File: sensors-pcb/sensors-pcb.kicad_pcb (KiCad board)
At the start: 2 copper layers, 75 x 55 mm, 67 parts, among them J1 Network Connector, J2 STDC14, J3 Conn_Coaxial, SW1 SW_Push, U1 MAX-M8Q, U2 BNO055, U3 LD39050PU33R, U4 STM32G474RBT6, U5 SN65HVD230, Y1 32kHz, Y2 8MHz

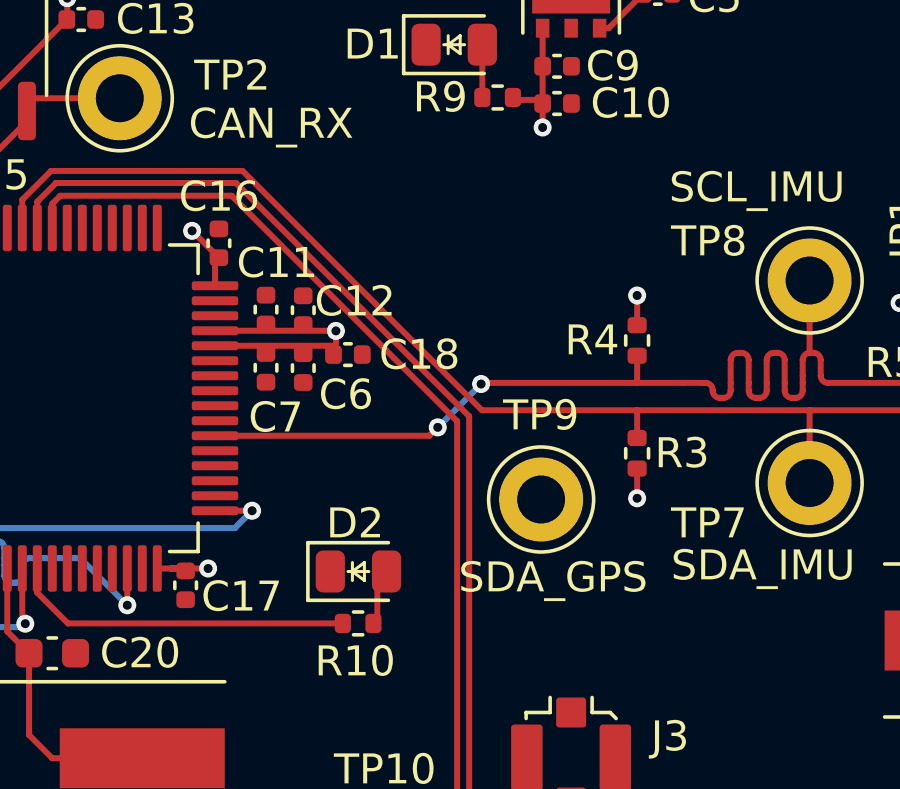
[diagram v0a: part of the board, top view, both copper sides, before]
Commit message: sensors-pcb: connector SDA_GPS test point
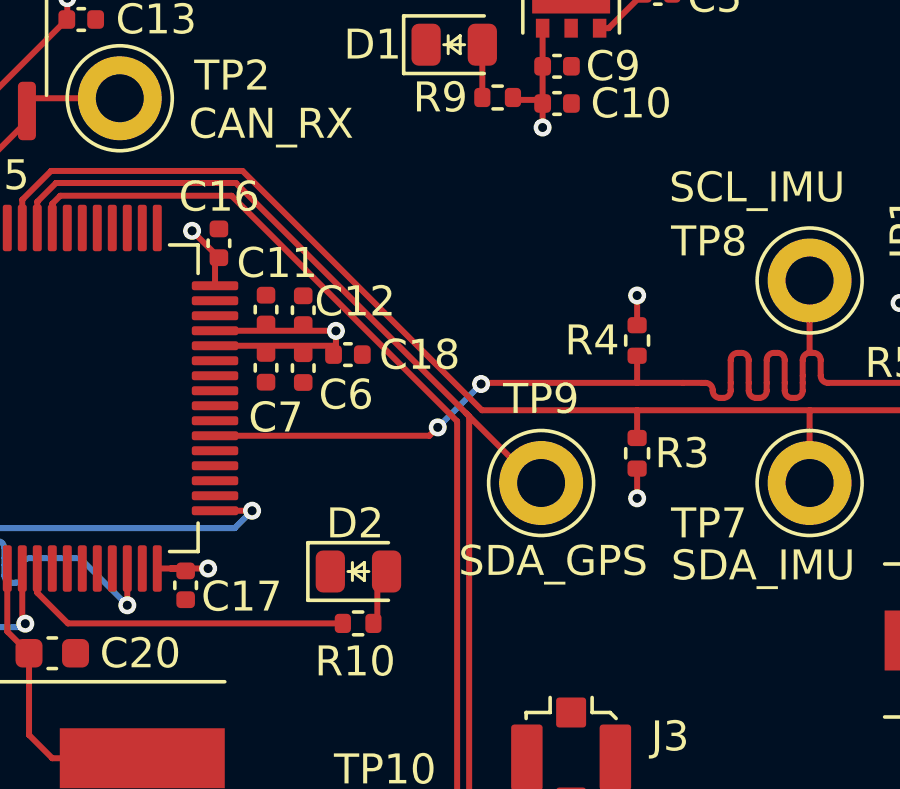
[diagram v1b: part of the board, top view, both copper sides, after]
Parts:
- moved TP9 0.55 mm to (234.8, 50.2)
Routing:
- net /SDA_GPS: track 44.6 -> 48.0 mm
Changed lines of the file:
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@@
 	(footprint "TestPoint:TestPoint_Keystone_5005-5009_Compact"
 		(layer "F.Cu")
-		(at 234.8 50.8)
+		(at 234.8 50.25)
 		(descr "Keystone THM Compact Test Point 5005-5009, http://www.keyelco.com/product-pdf.cfm?p=1314")
 		(tags "Through Hole Mount Test Points")
@@
 	)
 	(segment
+		(start 232.312325 47.937675)
+		(end 232.401 48.02635)
+		(width 0.2)
+		(layer "F.Cu")
+		(net 37)
+	)
+	(segment
 		(start 232.401 48.02635)
 		(end 232.401 64.826339)
@@
 	(segment
 		(start 224.62465 40.25)
-		(end 232.401 48.02635)
+		(end 232.312325 47.937675)
+		(width 0.2)
+		(layer "F.Cu")
+		(net 37)
+	)
+	(segment
+		(start 232.312325 47.937675)
+		(end 234.62465 50.25)
 		(width 0.2)
 		(layer "F.Cu")
@@
 		(width 0.2)
 		(layer "F.Cu")
+		(net 37)
+	)
+	(segment
+		(start 234.62465 50.25)
+		(end 234.8 50.25)
+		(width 0.2)
+		(layer "F.Cu")

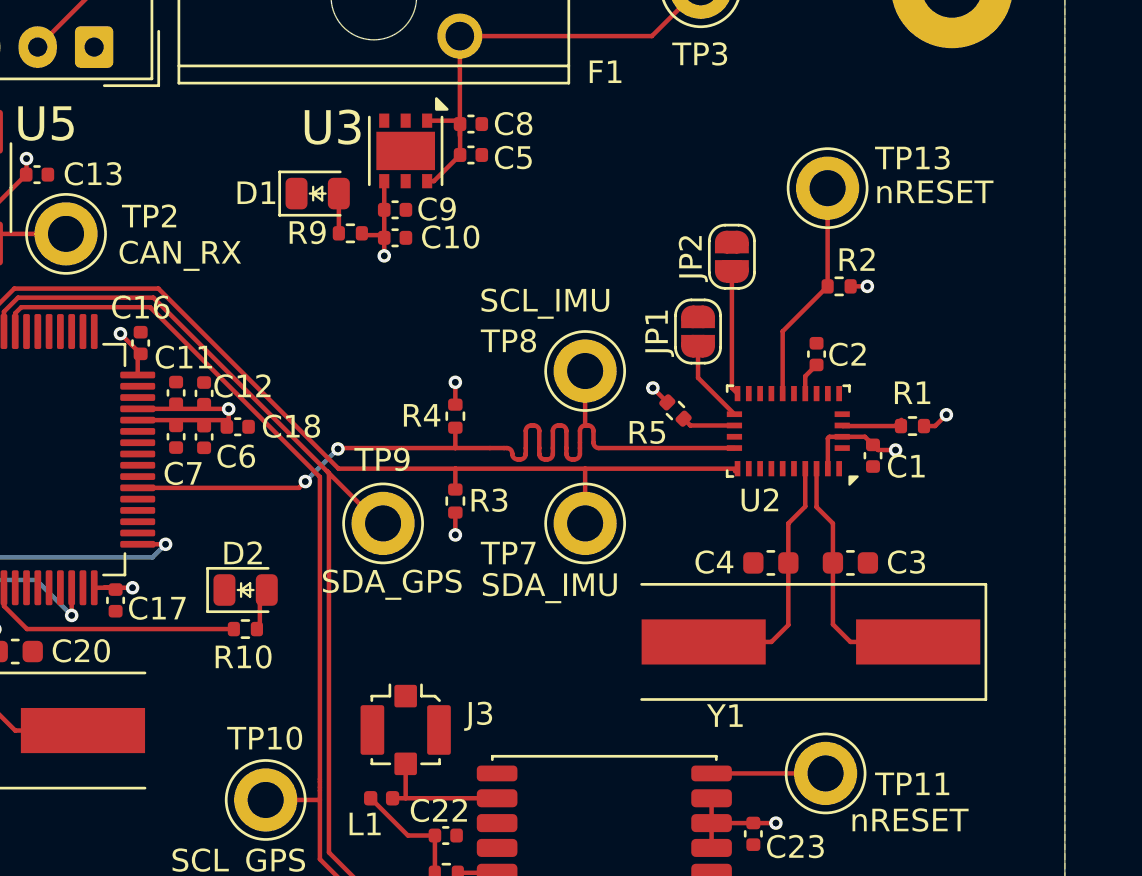
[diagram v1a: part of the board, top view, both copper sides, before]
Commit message: sensors-pcb: replace IMU with MPU-6050
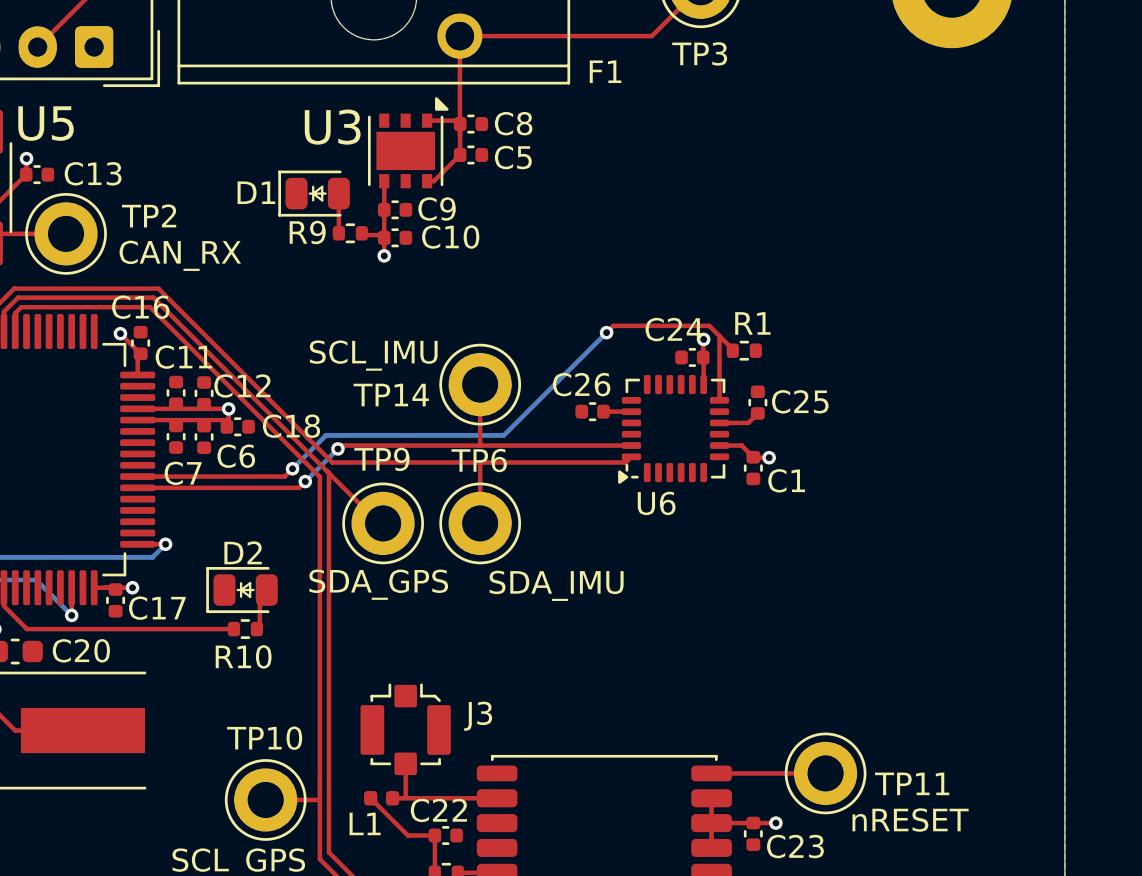
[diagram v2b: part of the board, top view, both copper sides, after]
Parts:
- removed C2: 100n, Capacitor_SMD:C_0402_1005Metric
- removed C3, C4: 22p, Capacitor_SMD:C_0603_1608Metric
- removed JP1, JP2: SolderJumper_2_Open, Jumper:SolderJumper-2_P1.3mm_Open_RoundedPad1.0x1.5mm
- removed R2, R3, R4: 10k, Resistor_SMD:R_0402_1005Metric
- removed R5: 39k, Resistor_SMD:R_0402_1005Metric
- removed TP13, TP7, TP8: TestPoint, TestPoint:TestPoint_Keystone_5005-5009_Compact
- removed U2: BNO055, Package_LGA:LGA-28_5.2x3.8mm_P0.5mm
- removed Y1: 32kHz, Exocet:Crystal_SMD_HC49-SD
- added C24: 100n, Capacitor_SMD:C_0402_1005Metric, F.Cu at (248.5, 42.9)
- added C25: 100n, Capacitor_SMD:C_0402_1005Metric, F.Cu at (251.4, 44.9)
- added C26: 2.2n, Capacitor_SMD:C_0402_1005Metric, F.Cu at (244.1, 45.3)
- added TP14: TestPoint, TestPoint:TestPoint_Keystone_5005-5009_Compact, F.Cu at (239.1, 44.1)
- added TP6: TestPoint, TestPoint:TestPoint_Keystone_5005-5009_Compact, F.Cu at (239.1, 50.2)
- added U6: MPU-6050, Sensor_Motion:InvenSense_QFN-24_4x4mm_P0.5mm, F.Cu at (247.8, 46.0)
- C1: value 100n -> 10n
- R1: value 10k -> 100k
- moved R1 8.16 mm to (250.8, 42.6)
- moved C1 5.33 mm to (251.2, 47.8), turned to 90 degrees
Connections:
- C1 pad 1: +3.3V -> GND
- C1 pad 2: GND -> +3.3V
- R1 pad 1: Net-(U2-nBOOT_LOAD_PIN) -> /INT_IMU
- R1 pad 2: +3.3V -> GND
- U4 pad 23: unconnected-(U4-PC5-Pad23) -> /INT_IMU
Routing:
- net /INT_IMU: track 0.00 -> 32.5 mm, vias 0 -> 2
- net /SCL_IMU: track 37.9 -> 25.3 mm
- net /OSC_IN: track 11.6 -> 0.00 mm
- net /OSC_OUT: track 11.6 -> 0.00 mm
- net Net-(U2-~{nReset}): track 9.92 -> 0.00 mm
- net /SDA_IMU: track 41.1 -> 35.6 mm
- net Net-(JP2-A): track 5.52 -> 0.00 mm
- net +3.3V: track 44.9 -> 39.9 mm, vias 16 -> 12
- net Net-(JP1-A): track 3.68 -> 0.00 mm
- net Net-(U2-nBOOT_LOAD_PIN): track 2.97 -> 0.00 mm
- net Net-(U2-COM3): track 2.38 -> 0.00 mm
- net Net-(U6-REGOUT): track 0.00 -> 1.87 mm
- net Net-(U2-CAP): track 1.48 -> 0.00 mm
- net Net-(U6-CPOUT): track 0.00 -> 1.24 mm

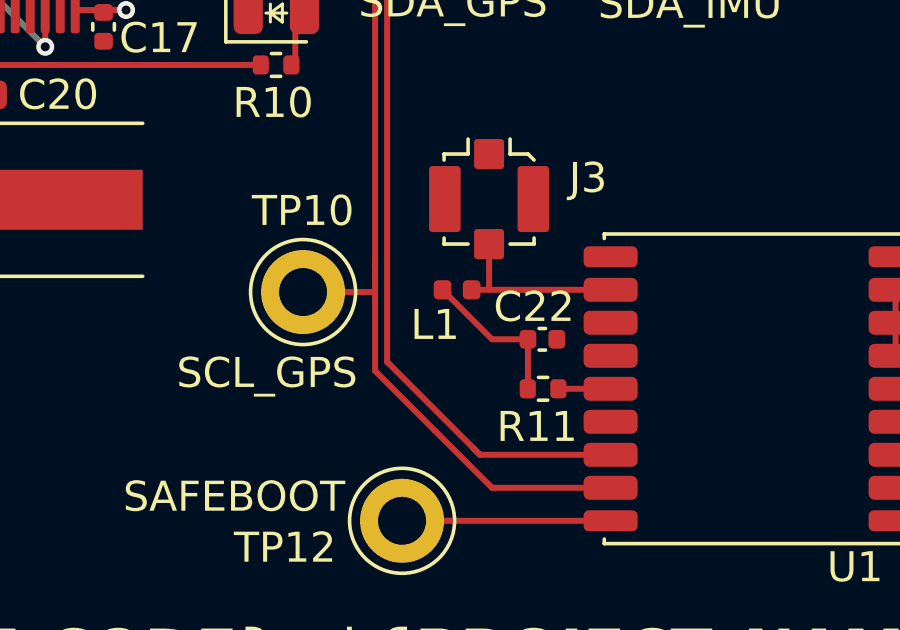
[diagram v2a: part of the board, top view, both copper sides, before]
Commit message: sensors-pcb: change 27nH to 10nH+15nH
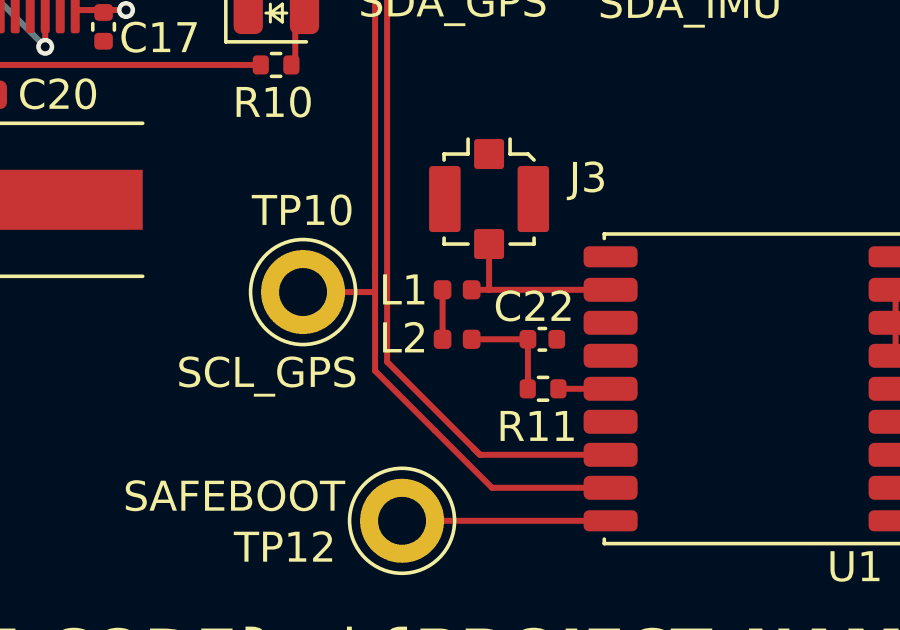
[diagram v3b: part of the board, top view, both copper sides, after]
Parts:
- added L2: 15n, Inductor_SMD:L_0402_1005Metric, F.Cu at (234.7, 64.1)
- L1: value 27n -> 10n
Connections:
- L1 pad 1: Net-(C22-Pad1) -> Net-(L1-Pad1)
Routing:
- net Net-(C22-Pad1): track 5.18 -> 3.53 mm
- net Net-(L1-Pad1): track 0.00 -> 1.65 mm
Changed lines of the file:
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@@
 	(net 94 "Net-(C22-Pad1)")
 	(net 95 "Net-(U1-~{SAFEBOOT})")
+	(net 96 "Net-(L1-Pad1)")
 	(footprint "Capacitor_SMD:C_0402_1005Metric"
 		(layer "F.Cu")
@@
 		(tags "inductor")
 		(property "Reference" "L1"
-			(at -0.735 1.175 0)
+			(at -1.785 0.025 0)
 			(layer "F.SilkS")
 			(effects
@@
 			)
 		)
-		(property "Value" "27n"
+		(property "Value" "10n"
 			(at 0 0 0)
 			(layer "F.Fab")
@@
 			)
 		)
-		(property "JLCPCB" "C12669"
+		(property "JLCPCB" "C27147"
 			(at 0 0 0)
 			(unlocked yes)
@@
 			(layers "F.Cu" "F.Mask" "F.Paste")
 			(roundrect_rratio 0.25)
-			(net 94 "Net-(C22-Pad1)")
+			(net 96 "Net-(L1-Pad1)")
 			(pinfunction "1")
 			(pintype "passive")
@@
 		)
 	)
+	(footprint "Inductor_SMD:L_0402_1005Metric"
+		(layer "F.Cu")
+		(at 234.735 64.075 180)
+		(descr "Inductor SMD 0402 (1005 Metric), square (rectangular) end terminal, IPC-7351 nominal, (Body size source: http://www.tortai-tech.com/upload/download/2011102023233369053.pdf), generated with kicad-footprint-generator")
+		(tags "inductor")
+		(property "Reference" "L2"
+			(at 1.785 0.025 0)
+			(layer "F.SilkS")
+			(effects
+				(font
+					(size 1 1)
+					(thickness 0.15)
+				)
+			)
+		)
+		(property "Value" "15n"
+			(at 0 0 0)
+			(layer "F.Fab")
+			(effects
+				(font
+					(size 1 1)
+					(thickness 0.15)
+				)
+			)
+		)
+		(property "Datasheet" "~"
+			(at 0 0 0)
+			(layer "F.Fab")
+			(hide yes)
+			(effects
+				(font
+					(size 1.27 1.27)
+					(thickness 0.15)
+				)
+			)
+		)
+		(property "Description" "Inductor"
+			(at 0 0 0)
+			(layer "F.Fab")
+			(hide yes)
+			(effects
+				(font
+					(size 1.27 1.27)
+					(thickness 0.15)
+				)
+			)
+		)
+		(property "JLCPCB" "C27143"
+			(at 0 0 180)
+			(unlocked yes)
+			(layer "F.Fab")
+			(hide yes)
+			(effects
+				(font
+					(size 1 1)
+					(thickness 0.15)
+				)
+			)
+		)
+		(property ki_fp_filters "Choke_* *Coil* Inductor_* L_*")
+		(sheetname "/")
+		(sheetfile "sensors-pcb.kicad_sch")
+		(attr smd)
+		(fp_line
+			(start 0.93 0.47)
+			(end -0.93 0.47)
+			(stroke
+				(width 0.05)
+				(type solid)
+			)
+			(layer "F.CrtYd")
+		)
+		(fp_line
+			(start 0.93 -0.47)
+			(end 0.93 0.47)
+			(stroke
+				(width 0.05)
+				(type solid)
+			)
+			(layer "F.CrtYd")
+		)
+		(fp_line
+			(start -0.93 0.47)
+			(end -0.93 -0.47)
+			(stroke
+				(width 0.05)
+				(type solid)
+			)
+			(layer "F.CrtYd")
+		)
+		(fp_line
+			(start -0.93 -0.47)
+			(end 0.93 -0.47)
+			(stroke
+				(width 0.05)
+				(type solid)
+			)
+			(layer "F.CrtYd")
+		)
+		(fp_line
+			(start 0.5 0.25)
+			(end -0.5 0.25)
+			(stroke
+				(width 0.1)
+				(type solid)
+			)
+			(layer "F.Fab")
+		)
+		(fp_line
+			(start 0.5 -0.25)
+			(end 0.5 0.25)
+			(stroke
+				(width 0.1)
+				(type solid)
+			)
+			(layer "F.Fab")
+		)
+		(fp_line
+			(start -0.5 0.25)
+			(end -0.5 -0.25)
+			(stroke
+				(width 0.1)
+				(type solid)
+			)
+			(layer "F.Fab")
+		)
+		(fp_line
+			(start -0.5 -0.25)
+			(end 0.5 -0.25)
+			(stroke
+				(width 0.1)
+				(type solid)
+			)
+			(layer "F.Fab")
+		)
+		(fp_text user "${REFERENCE}"
+			(at 0 0 0)
+			(layer "F.Fab")
+			(effects
+				(font
+					(size 0.25 0.25)
+					(thickness 0.04)
+				)
+			)
+		)
+		(pad "1" smd roundrect
+			(at -0.485 0 180)
+			(size 0.59 0.64)
+			(layers "F.Cu" "F.Mask" "F.Paste")
+			(roundrect_rratio 0.25)
+			(net 94 "Net-(C22-Pad1)")
+			(pinfunction "1")
+			(pintype "passive")
+		)
+		(pad "2" smd roundrect
+			(at 0.485 0 180)
+			(size 0.59 0.64)
+			(layers "F.Cu" "F.Mask" "F.Paste")
+			(roundrect_rratio 0.25)
+			(net 96 "Net-(L1-Pad1)")
+			(pinfunction "2")
+			(pintype "passive")
+		)
+		(embedded_fonts no)
+		(model "${KICAD9_3DMODEL_DIR}/Inductor_SMD.3dshapes/L_0402_1005Metric.step"
+			(offset
+				(xyz 0 0 0)
+			)
+			(scale
+				(xyz 1 1 1)
+			)
+			(rotate
+				(xyz 0 0 0)
+			)
+		)
+	)
 	(footprint "Resistor_SMD:R_0402_1005Metric"
 		(layer "F.Cu")
@@
 	)
 	(segment
-		(start 237.095 64.075)
-		(end 237.095 65.720001)
-		(width 0.2)
-		(layer "F.Cu")
-		(net 94)
-	)
-	(segment
-		(start 234.25 62.425)
-		(end 235.9 64.075)
+		(start 235.22 64.075)
+		(end 237.095 64.075)
 		(width 0.2)
 		(layer "F.Cu")
@@
 	)
 	(segment
-		(start 235.9 64.075)
-		(end 237.095 64.075)
+		(start 237.095 64.075)
+		(end 237.095 65.720001)
 		(width 0.2)
 		(layer "F.Cu")
@@
 		(net 95)
 	)
+	(segment
+		(start 234.25 62.425)
+		(end 234.25 64.075)
+		(width 0.2)
+		(layer "F.Cu")
+		(net 96)
+	)
 	(zone

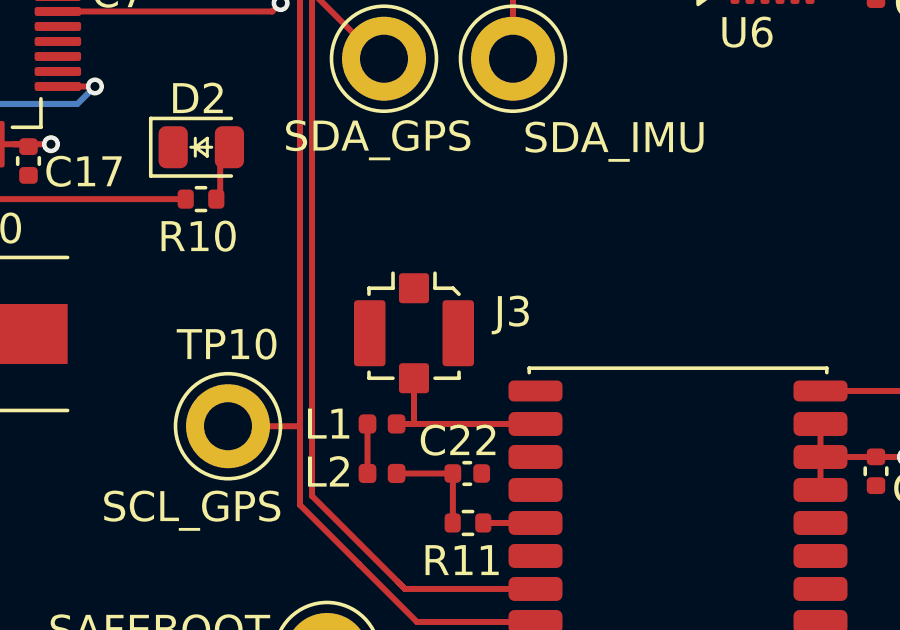
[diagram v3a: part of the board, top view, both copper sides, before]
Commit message: sensors-pcb: change antenna coax connector
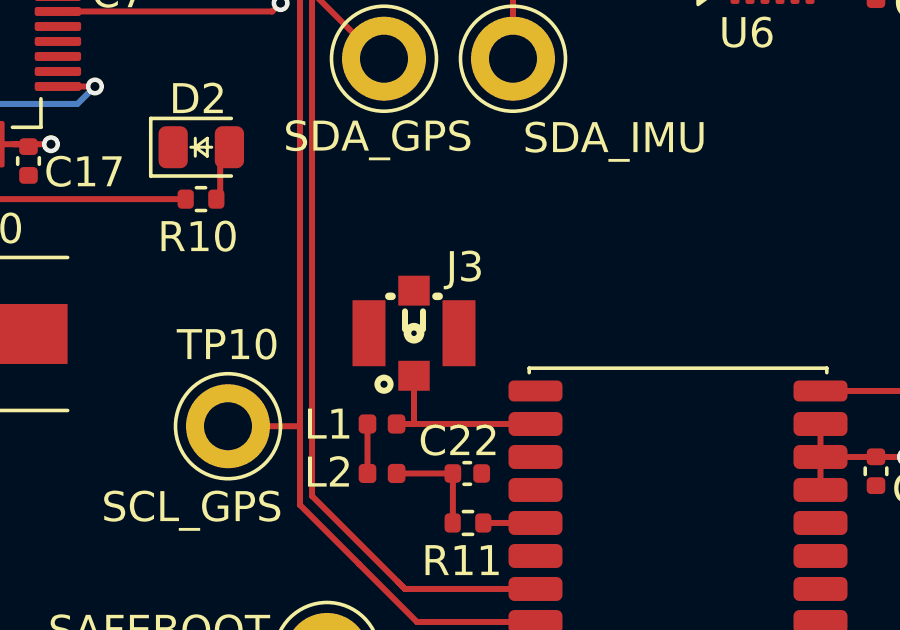
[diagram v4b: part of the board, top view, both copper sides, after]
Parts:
- J3: footprint Connector_Coaxial:U.FL_Molex_MCRF_73412-0110_Vertical -> Exocet:ANT-SMD_KH-IPEX-K501-29
